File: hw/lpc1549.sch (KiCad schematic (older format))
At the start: 17 parts, among them J301 ARM_JTAG_SWD_HEADER_10_PINSMD, U302 LPC1549JBD64, X301 XTAL_7A-12.000MAAJ-T

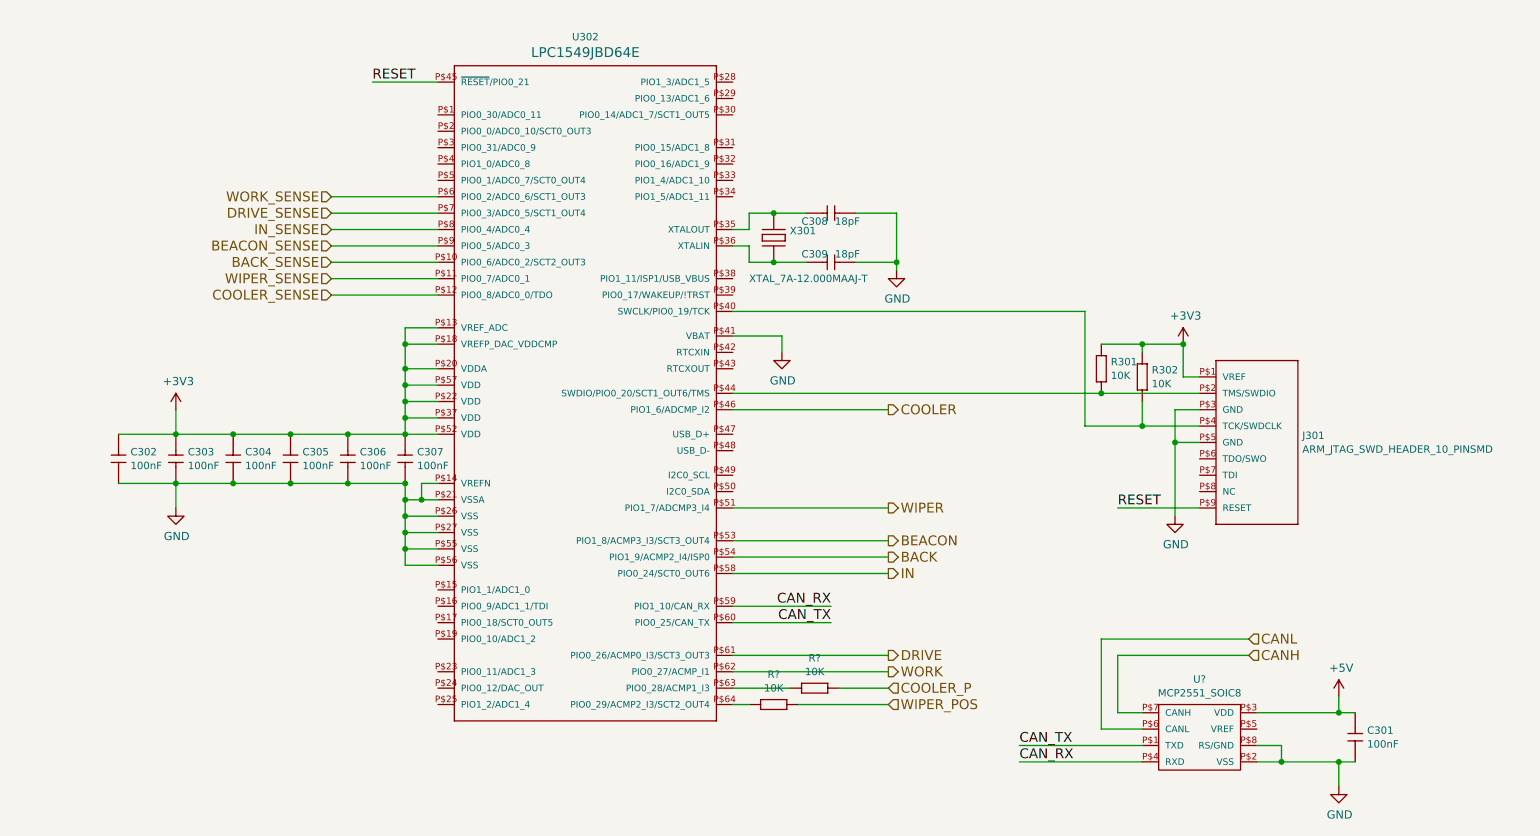
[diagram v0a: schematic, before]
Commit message: first pcb revision ready to order
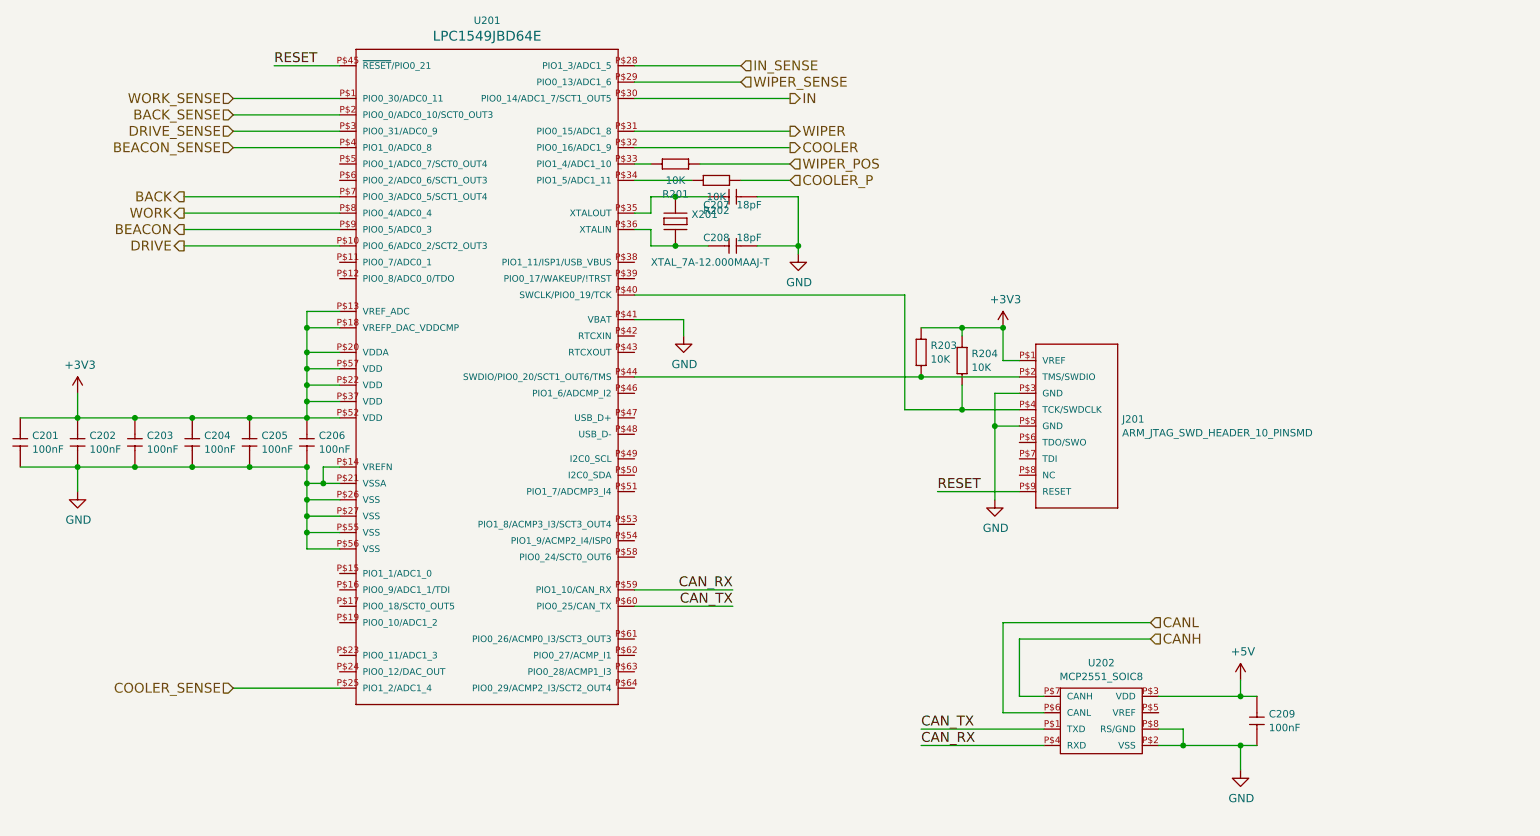
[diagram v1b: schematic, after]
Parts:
- gave numbers to parts that had none: 3
- renumbered C302 to C201, C303 to C202, C304 to C203, C305 to C204, C306 to C205, C307 to C206, C308 to C207, C309 to C208, C301 to C209, J301 to J201, R301 to R203, R302 to R204, U302 to U201, X301 to X201
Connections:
- net BACK: now also U201.P$7 (PIO0_3/ADC0_5/SCT1_OUT4); no longer U201.P$54 (PIO1_9/ACMP2_I4/ISP0)
- net BACK_SENSE: now also U201.P$2 (PIO0_0/ADC0_10/SCT0_OUT3); no longer U201.P$10 (PIO0_6/ADC0_2/SCT2_OUT3)
- net BEACON: now also U201.P$9 (PIO0_5/ADC0_3); no longer U201.P$53 (PIO1_8/ACMP3_I3/SCT3_OUT4)
- net BEACON_SENSE: now also U201.P$4 (PIO1_0/ADC0_8); no longer U201.P$9 (PIO0_5/ADC0_3)
- net COOLER: now also U201.P$32 (PIO0_16/ADC1_9); no longer U201.P$46 (PIO1_6/ADCMP_I2)
- net COOLER_SENSE: now also U201.P$25 (PIO1_2/ADC1_4); no longer U201.P$12 (PIO0_8/ADC0_0/TDO)
- net DRIVE: now also U201.P$10 (PIO0_6/ADC0_2/SCT2_OUT3); no longer U201.P$61 (PIO0_26/ACMP0_I3/SCT3_OUT3)
- net DRIVE_SENSE: now also U201.P$3 (PIO0_31/ADC0_9); no longer U201.P$7 (PIO0_3/ADC0_5/SCT1_OUT4)
- net IN: now also U201.P$30 (PIO0_14/ADC1_7/SCT1_OUT5); no longer U201.P$58 (PIO0_24/SCT0_OUT6)
- net IN_SENSE: now also U201.P$28 (PIO1_3/ADC1_5); no longer U201.P$8 (PIO0_4/ADC0_4)
- net WIPER: now also U201.P$31 (PIO0_15/ADC1_8); no longer U201.P$51 (PIO1_7/ADCMP3_I4)
- net WIPER_SENSE: now also U201.P$29 (PIO0_13/ADC1_6); no longer U201.P$11 (PIO0_7/ADC0_1)
- net WORK: now also U201.P$8 (PIO0_4/ADC0_4); no longer U201.P$62 (PIO0_27/ACMP_I1)
- net WORK_SENSE: now also U201.P$1 (PIO0_30/ADC0_11); no longer U201.P$6 (PIO0_2/ADC0_6/SCT1_OUT3)
- net at U201.P$33 (PIO1_4/ADC1_10): now also R201.2 (R2)
- net at U201.P$34 (PIO1_5/ADC1_11): now also R202.2 (R2)
- net at U201.P$63 (PIO0_28/ACMP1_I3): no longer R202.2 (R2)
- net at U201.P$64 (PIO0_29/ACMP2_I3/SCT2_OUT4): no longer R201.2 (R2)
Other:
- moved on the sheet: C201, C202, C203, C204, C205, C206, C207, C208, C209, J201, R201, R202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

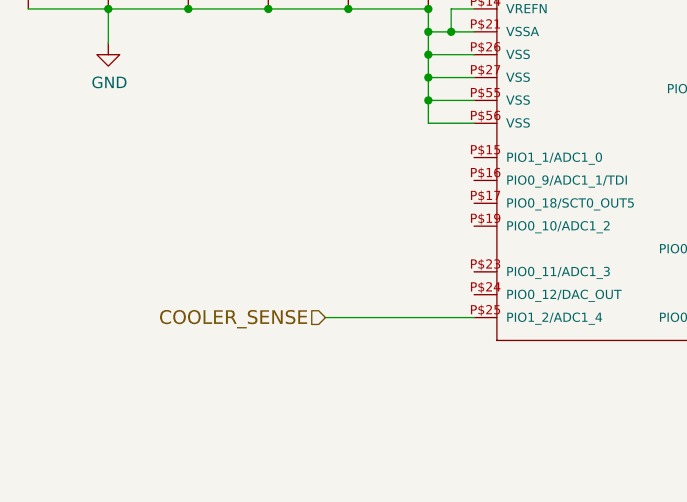
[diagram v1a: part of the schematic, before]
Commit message: sw directory created, oil cooler added in hw
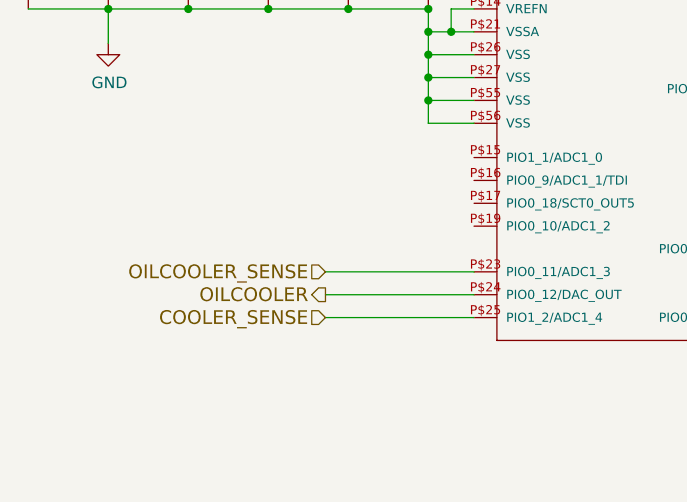
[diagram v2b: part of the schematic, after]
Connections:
- net OILCOOLER_SENSE: now reaches U201.P$23 (PIO0_11/ADC1_3)
- net OILCOOLER: now reaches U201.P$24 (PIO0_12/DAC_OUT)
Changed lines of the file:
@@
 $Descr A4 11693 8268
 encoding utf-8
-Sheet 2 12
+Sheet 13 13
 Title ""
 Date ""
@@
 $EndComp
 $Comp
-L +3V3 #PWR06
+L +3V3 #PWR035
 U 1 1 57E689A3
 P 3000 3850
-F 0 "#PWR06" H 3000 3700 50  0001 C CNN
+F 0 "#PWR035" H 3000 3700 50  0001 C CNN
 F 1 "+3V3" H 3015 4023 50  0000 C CNN
 F 2 "" H 3000 3850 50  0000 C CNN
@@
 $EndComp
 $Comp
-L GND #PWR07
+L GND #PWR036
 U 1 1 57E689C9
 P 3000 4450
-F 0 "#PWR07" H 3000 4200 50  0001 C CNN
+F 0 "#PWR036" H 3000 4200 50  0001 C CNN
 F 1 "GND" H 3005 4277 50  0000 C CNN
 F 2 "" H 3000 4450 50  0000 C CNN
@@
 $EndComp
 $Comp
-L GND #PWR08
+L GND #PWR037
 U 1 1 57E697A1
 P 7400 3000
-F 0 "#PWR08" H 7400 2750 50  0001 C CNN
+F 0 "#PWR037" H 7400 2750 50  0001 C CNN
 F 1 "GND" H 7405 2827 50  0000 C CNN
 F 2 "" H 7400 3000 50  0000 C CNN
@@
 $EndComp
 $Comp
-L GND #PWR09
+L GND #PWR038
 U 1 1 57E69A8B
 P 6700 3500
-F 0 "#PWR09" H 6700 3250 50  0001 C CNN
+F 0 "#PWR038" H 6700 3250 50  0001 C CNN
 F 1 "GND" H 6705 3327 50  0000 C CNN
 F 2 "" H 6700 3500 50  0000 C CNN
@@
 $EndComp
 $Comp
-L GND #PWR010
+L GND #PWR039
 U 1 1 5891FBFB
 P 8600 4500
-F 0 "#PWR010" H 8600 4250 50  0001 C CNN
+F 0 "#PWR039" H 8600 4250 50  0001 C CNN
 F 1 "GND" H 8605 4327 50  0000 C CNN
 F 2 "" H 8600 4500 50  0000 C CNN
@@
 $EndComp
 $Comp
-L +3V3 #PWR011
+L +3V3 #PWR040
 U 1 1 5891FCDE
 P 8650 3450
-F 0 "#PWR011" H 8650 3300 50  0001 C CNN
+F 0 "#PWR040" H 8650 3300 50  0001 C CNN
 F 1 "+3V3" H 8665 3623 50  0000 C CNN
 F 2 "" H 8650 3450 50  0000 C CNN
@@
 Connection ~ 8650 3450
 $Comp
-L GND #PWR012
+L GND #PWR041
 U 1 1 58C01588
 P 10100 6150
-F 0 "#PWR012" H 10100 5900 50  0001 C CNN
+F 0 "#PWR041" H 10100 5900 50  0001 C CNN
 F 1 "GND" H 10105 5977 50  0000 C CNN
 F 2 "" H 10100 6150 50  0000 C CNN
@@
 	10200 5700 9600 5700
 $Comp
-L +5V #PWR013
+L +5V #PWR042
 U 1 1 595E0BE4
 P 10100 5600
-F 0 "#PWR013" H 10100 5450 50  0001 C CNN
+F 0 "#PWR042" H 10100 5450 50  0001 C CNN
 F 1 "+5V" H 10115 5773 50  0000 C CNN
 F 2 "" H 10100 5600 50  0000 C CNN
@@
 	10100 5600 10100 5700
 Connection ~ 10100 5700
+Wire Wire Line
+	4600 5450 3950 5450
+Text HLabel 3950 5450 0    60   Input ~ 0
+OILCOOLER_SENSE
+Wire Wire Line
+	4600 5550 3950 5550
+Text HLabel 3950 5550 0    60   Output ~ 0
+OILCOOLER
 $EndSCHEMATC
